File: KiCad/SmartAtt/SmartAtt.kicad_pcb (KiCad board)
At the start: 2 copper layers, 109.9 x 107.2 mm, 17 parts, among them IC1 74LVC4245APW,112, J16 CON1, J17 CON1, J8 CON1, J9 CON1, U1 ESP32-WROOM-32E, U2 HMC542BLP4ETR

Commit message: schematic finished. Need footprint to be added
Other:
- board text removed: "LBON LKB"
- board text removed: "РМВА.758725.005, изм."

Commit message: contur added
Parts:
- removed the ? at (93.9, 68.9)
- removed the ? at (190.0, 68.9)
- removed the ? at (190.0, 121.1)
- removed the ? at (93.9, 121.1)
- removed C1: 10N, C__Documents and Settings_All Users_Äîêóìåíòû_Altium_AD13_Library_Miscellaneous Devices.IntLib:6-0805_N
- removed IC1: 74LVC4245APW,112, Shar_Library:SOP65P640X110-24N
- removed R1: 75/50, C__Documents and Settings_All Users_Äîêóìåíòû_Altium_AD13_Library_Miscellaneous Devices.IntLib:6-0805_N
- removed U1: ESP32-WROOM-32E, RF_Module:ESP32-WROOM-32D
- removed U2: HMC542BLP4ETR, Package_DFN_QFN:QFN-24-1EP_4x4mm_P0.5mm_EP2.6x2.6mm_ThermalVias
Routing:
- net (no net): track 62.4 -> 11.1 mm, vias 15 -> 0
- removed copper zone on B.Cu, net (none)
- removed copper zone on F.Cu, net (none)
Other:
- outline, holes or cut-outs redrawn

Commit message: ...
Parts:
- removed ? (x4): , 
- removed J16, J17, J8, J9: CON1, VIA
- added BZ1: Buzzer, Alexeyj4:HC0903A, F.Cu at (121.8, 44.9)
- added C1: 2,2 нФ, Capacitor_THT:C_Disc_D10.0mm_W2.5mm_P5.00mm, B.Cu at (126.8, 90.7)
- added C10: 330 пФ, Capacitor_SMD:C_0805_2012Metric_Pad1.18x1.45mm_HandSolder, B.Cu at (161.2, 84.8)
- added C11: 47 мкФ, Capacitor_Tantalum_SMD:CP_EIA-7343-31_Kemet-D_Pad2.25x2.55mm_HandSolder, B.Cu at (174.7, 103.3)
- added C12: 100 нФ, Capacitor_SMD:C_0805_2012Metric_Pad1.18x1.45mm_HandSolder, B.Cu at (195.0, 57.2)
- added C13: 47 мкФ, Capacitor_Tantalum_SMD:CP_EIA-7343-31_Kemet-D_Pad2.25x2.55mm_HandSolder, B.Cu at (162.7, 103.2)
- added C14: 100 нФ, Capacitor_SMD:C_0805_2012Metric_Pad1.18x1.45mm_HandSolder, B.Cu at (182.8, 57.2)
- added C15: 100 нФ, Capacitor_SMD:C_0805_2012Metric_Pad1.18x1.45mm_HandSolder, B.Cu at (181.8, 40.8)
- added C16: 2,2 нФ, Capacitor_THT:C_Disc_D10.0mm_W2.5mm_P5.00mm, B.Cu at (190.4, 90.7)
- added C2: 47 мкФ, Capacitor_Tantalum_SMD:CP_EIA-7343-31_Kemet-D_Pad2.25x2.55mm_HandSolder, B.Cu at (136.8, 138.6)
- added C3: 47 мкФ, Capacitor_Tantalum_SMD:CP_EIA-7343-31_Kemet-D_Pad2.25x2.55mm_HandSolder, B.Cu at (136.8, 121.0)
- added C4: 47 мкФ, Capacitor_Tantalum_SMD:CP_EIA-7343-31_Kemet-D_Pad2.25x2.55mm_HandSolder, B.Cu at (148.0, 134.4)
- added C5: 47 мкФ, Capacitor_Tantalum_SMD:CP_EIA-7343-31_Kemet-D_Pad2.25x2.55mm_HandSolder, B.Cu at (175.2, 132.2)
- added C6: 47 мкФ, Capacitor_Tantalum_SMD:CP_EIA-7343-31_Kemet-D_Pad2.25x2.55mm_HandSolder, B.Cu at (149.3, 98.9)
- added C7: 330 пФ, Capacitor_SMD:C_0805_2012Metric_Pad1.18x1.45mm_HandSolder, B.Cu at (151.9, 84.8)
- added C8: 330 пФ, Capacitor_SMD:C_0805_2012Metric_Pad1.18x1.45mm_HandSolder, B.Cu at (155.0, 84.8)
- added C9: 330 пФ, Capacitor_SMD:C_0805_2012Metric_Pad1.18x1.45mm_HandSolder, B.Cu at (158.0, 84.8)
- added D1: 10BQ040, Diode_SMD:D_SMB_Handsoldering, B.Cu at (83.2, 135.5)
- added D2: 10BQ040, Diode_SMD:D_SMB_Handsoldering, B.Cu at (93.8, 135.5)
- added D3: 10BQ040, Diode_SMD:D_SMB_Handsoldering, B.Cu at (93.7, 130.4)
- added D4: LED, LED_SMD:LED_1206_3216Metric_Pad1.42x1.75mm_HandSolder, F.Cu at (101.0, 42.8)
- added IC1: 74LVC4245APW,112, Alexeyj4:SOP65P640X110-24N, B.Cu at (168.1, 111.7)
- added J1: RF_base, TestPoint:TestPoint_Pad_1.0x1.0mm, F.Cu at (80.3, 90.6)
- added J2: RF_base_gnd, TestPoint:TestPoint_Pad_1.0x1.0mm, F.Cu at (65.4, 104.0)
- added J3: 12V, Connector_JST:JST_PH_B2B-PH-K_1x02_P2.00mm_Vertical, F.Cu at (71.1, 138.2)
- added J4: UART_FW, Connector_PinHeader_2.54mm:PinHeader_1x04_P2.54mm_Vertical, F.Cu at (222.0, 139.4)
- added J5: RF_mine, TestPoint:TestPoint_Pad_1.0x1.0mm, F.Cu at (222.8, 90.7)
- added J6: RF_mine_gnd, TestPoint:TestPoint_Pad_1.0x1.0mm, F.Cu at (237.4, 104.2)
- added JP1: FW, Connector_PinHeader_2.54mm:PinHeader_1x03_P2.54mm_Vertical, F.Cu at (237.8, 134.6)
- added L1: 4 мГн мин., Inductor_THT:L_Axial_L24.0mm_D7.1mm_P30.48mm_Horizontal_Vishay_IM-10-28, B.Cu at (91.0, 95.5)
- added L2: 4 мГн мин., Inductor_THT:L_Axial_L24.0mm_D7.1mm_P30.48mm_Horizontal_Vishay_IM-10-28, B.Cu at (213.0, 97.0)
- added R1: 10 кОм, Resistor_SMD:R_0805_2012Metric_Pad1.20x1.40mm_HandSolder, B.Cu at (175.2, 126.0)
- added R2: 10 кОм, Resistor_SMD:R_0805_2012Metric_Pad1.20x1.40mm_HandSolder, B.Cu at (205.5, 117.5)
- added R3: 0 Ом, Resistor_SMD:R_0805_2012Metric_Pad1.20x1.40mm_HandSolder, B.Cu at (148.5, 46.0)
- added R4: 1 кОм, Resistor_SMD:R_0805_2012Metric_Pad1.20x1.40mm_HandSolder, B.Cu at (177.0, 108.5)
- added R5: NU, Resistor_SMD:R_0805_2012Metric_Pad1.20x1.40mm_HandSolder, B.Cu at (148.5, 50.0)
- added R6: 1 кОм, Resistor_SMD:R_0805_2012Metric_Pad1.20x1.40mm_HandSolder, B.Cu at (99.5, 48.6)
- added R7: 100 Ом, Resistor_SMD:R_0805_2012Metric_Pad1.20x1.40mm_HandSolder, B.Cu at (119.8, 50.2)
- added S1: EC11, Alexeyj4:RotaryEncoder EC11 SMD, F.Cu at (188.7, 48.2)
- added U1: MP-N, Alexeyj4:MPN, F.Cu at (131.0, 132.0)
- added U2: AMS1117-3.3, Package_TO_SOT_SMD:SOT-223-3_TabPin2, B.Cu at (136.6, 130.1)
- added U3: ESP32-WROOM-32E, RF_Module:ESP32-WROOM-32D, B.Cu at (191.4, 125.9)
- added U4: HMC542BLP4ETR, Package_DFN_QFN:QFN-24-1EP_4x4mm_P0.5mm_EP2.6x2.6mm_ThermalVias, B.Cu at (155.5, 91.0)
- added U5: OLED, Alexeyj4:OLED I2C, F.Cu at (151.2, 53.5)
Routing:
- net GND: track 0.00 -> 397.1 mm, vias 0 -> 4
- net +3.3V: track 0.00 -> 131.6 mm, vias 0 -> 5
- net Net-(JP1-A): track 0.00 -> 46.3 mm
- net Net-(J1-Pin_1): track 0.00 -> 43.5 mm, vias 0 -> 2
- net Net-(D1-K): track 0.00 -> 39.7 mm
- net +5V: track 0.00 -> 33.9 mm
- net /TX0: track 0.00 -> 30.7 mm
- net Net-(J5-Pin_1): track 0.00 -> 29.6 mm, vias 0 -> 2
- net /RX0: track 0.00 -> 28.7 mm, vias 0 -> 2
- net Net-(U4-RF2): track 0.00 -> 28.0 mm
- net Net-(U4-RF1): track 0.00 -> 26.8 mm
- net (no net): track 11.1 -> 0.00 mm, vias 0 -> 6
- net Net-(U5-VCC): track 0.00 -> 10.3 mm
- net Net-(U3-EN): track 0.00 -> 8.71 mm
- net Net-(U4-Vcc): track 0.00 -> 6.58 mm
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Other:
- board size 109.9 x 107.2 mm -> 207 x 107.2 mm

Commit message: pochti zakonchil razvodku
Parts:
- moved C16 23.5 mm to (166.9, 90.7)
- moved C1 22.2 mm to (148.9, 90.8)
- moved L2 12.2 mm to (212.8, 84.8), turned to 90 degrees
- moved L1 10.9 mm to (90.8, 84.6), turned to 90 degrees
- moved C11 3.83 mm to (171.0, 102.3), turned to 90 degrees
- moved C13 3.13 mm to (165.7, 102.3), turned to 90 degrees
- moved C6 1.00 mm to (149.3, 99.9)
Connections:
- C6 pad 1: Net-(U4-Vcc) -> +5V
- U4 pad 2: Net-(U4-Vcc) -> +5V
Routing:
- net GND: track 397.1 -> 115.9 mm, vias 4 -> 23
- net /Vline: track 4.47 -> 248.1 mm
- net +5V: track 33.9 -> 182.5 mm, vias 0 -> 5
- net /LED: track 0.00 -> 137.0 mm, vias 0 -> 8
- net /BUZ: track 0.00 -> 118.0 mm, vias 0 -> 6
- net /OLED_SCL: track 0.00 -> 113.2 mm, vias 0 -> 6
- net /OLED_SDA: track 0.00 -> 109.0 mm, vias 0 -> 6
- net /ENC_BTN: track 0.00 -> 94.5 mm, vias 0 -> 7
- net +3.3V: track 131.6 -> 218.4 mm
- net /ENC_B: track 0.00 -> 82.4 mm, vias 0 -> 7
- net /ENC_A: track 0.00 -> 75.0 mm, vias 0 -> 7
- net Net-(J5-Pin_1): track 29.6 -> 65.5 mm
- net /RESET_3V: track 0.00 -> 35.5 mm, vias 0 -> 2
- net /SH_CLK_3V: track 0.00 -> 35.1 mm, vias 0 -> 2
- net /LE_3V: track 0.00 -> 33.8 mm, vias 0 -> 2
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- added copper zone on F.Cu, net GND
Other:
- outline, holes or cut-outs redrawn

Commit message: finish pcb. Printing on paper
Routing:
- net GND: track 115.9 -> 131.9 mm
- net Net-(IC1-DIR): track 0.00 -> 6.26 mm
- net Net-(J1-Pin_1): track 74.0 -> 79.9 mm
- net Net-(U4-AGC1): track 5.12 -> 6.12 mm
- net /ENC_B: vias 7 -> 6
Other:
- board text added: "+"
- board text added: "-"
- board text added: "RF1"
- board text added: "RF2"
- board text added: "S/N: _________"
- board text added: "МАКСИМУМ +28 дБм 15 В DC"
- board text added: "ПИТАНИЕ 12 В"
- board text added: "УА-1 v1"

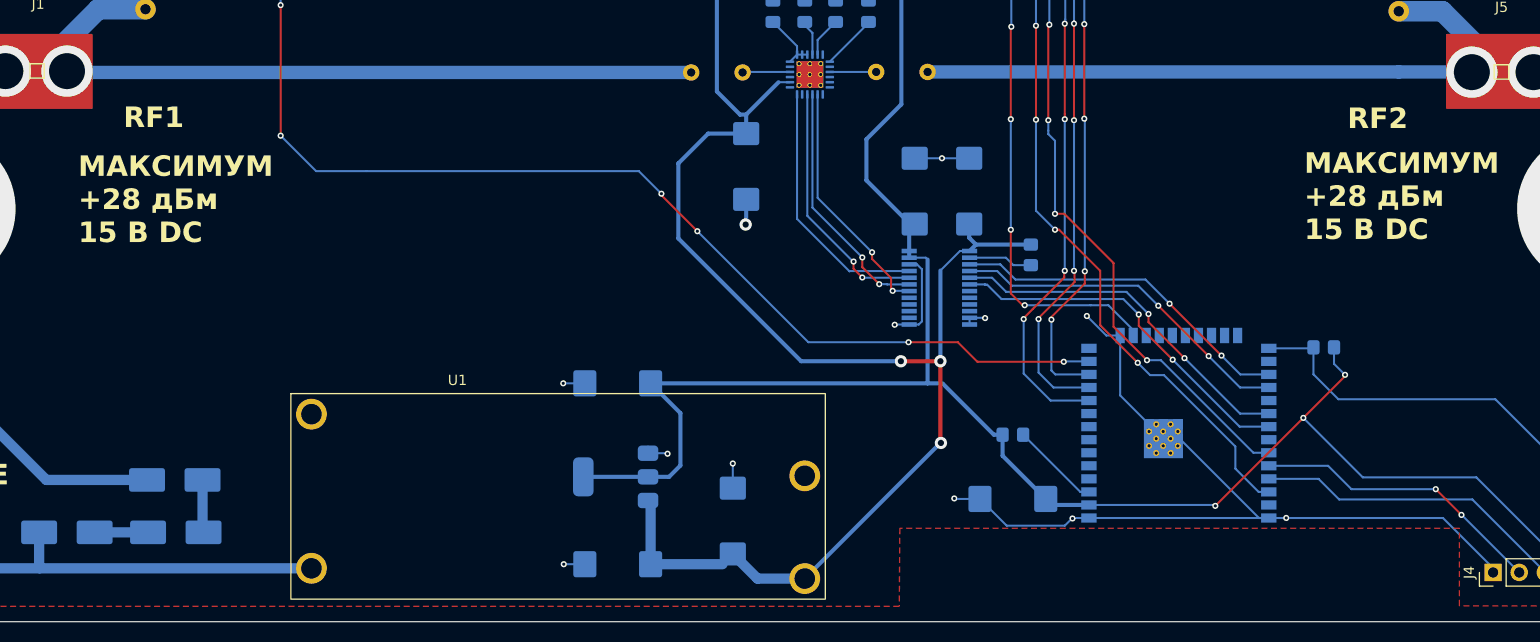
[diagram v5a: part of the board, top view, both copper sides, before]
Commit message: fix mpn gnd-5v. fix C 5-10mm
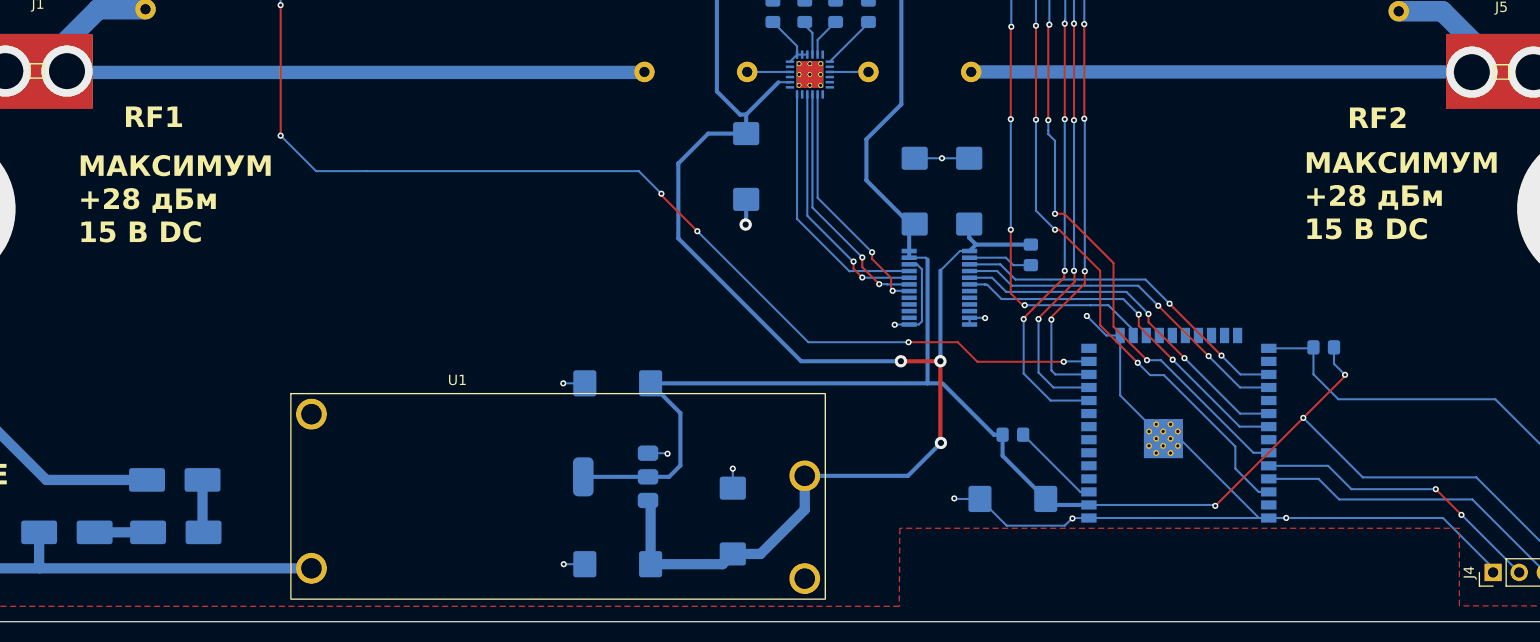
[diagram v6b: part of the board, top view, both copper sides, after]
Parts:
- C1, C16: footprint Capacitor_THT:C_Disc_D10.0mm_W2.5mm_P5.00mm -> Capacitor_THT:C_Disc_D7.5mm_W5.0mm_P10.00mm
- moved C16 4.25 mm to (171.2, 90.7)
- moved C1 0.45 mm to (149.4, 90.7)
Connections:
- U1 pad 3: GND -> +5V
- U1 pad 4: +5V -> GND
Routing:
- net Net-(J1-Pin_1): track 79.9 -> 75.4 mm
- net Net-(J5-Pin_1): track 65.5 -> 61.2 mm
- net Net-(U4-RF2): track 4.51 -> 3.76 mm
- net GND: track 131.9 -> 131.4 mm
